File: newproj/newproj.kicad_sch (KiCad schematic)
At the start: 1 part

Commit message: Add files via upload
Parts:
- removed U?: ESP32-WROOM-32, RF_Module:ESP32-WROOM-32, symbol RF_Module:ESP32-WROOM-32
- added U?: ESP32-S3-WROOM-2, RF_Module:ESP32-S3-WROOM-2, symbol New_Library:ESP32-S3-WROOM-2
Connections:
- new net AC: U?.1 (GND), U?.26 (IO45), U?.42 (GND), U?.43 (GND)
- new net LED_CONTROL: U?.4 (IO04)
- new net TEMP SENSOR 3.3V: U?.2 (3V3)
- new net TEMP SENSOR SIGNAL: U?.34 (IO41)
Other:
- removed sheet Heater
- removed sheet Power

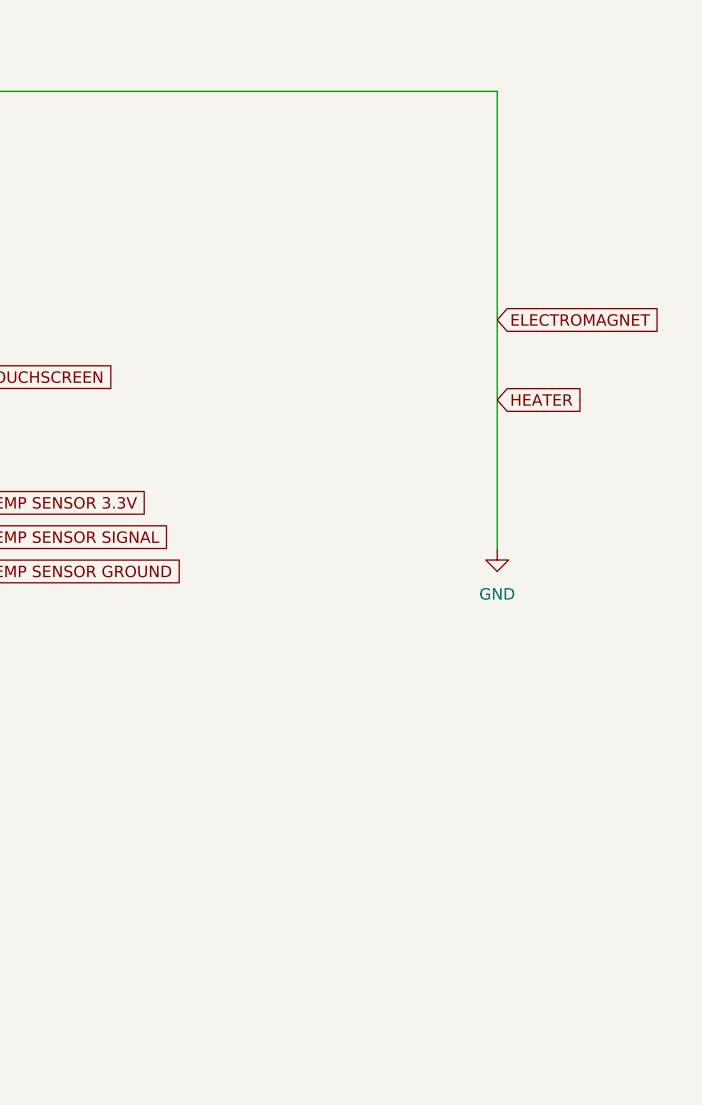
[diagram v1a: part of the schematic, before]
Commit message: Add display connector and change it in parts.txt
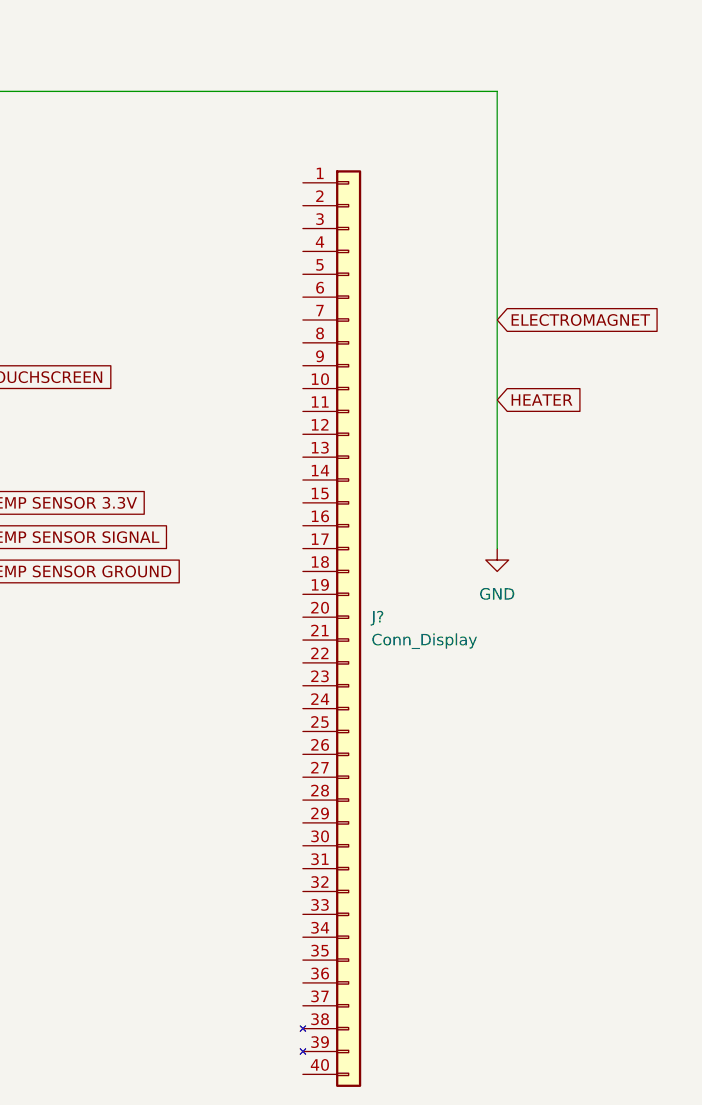
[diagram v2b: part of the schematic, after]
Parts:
- added J?: Conn_Display, symbol Conn_Display:Conn_Display
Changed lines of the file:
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@@
     )
+  )
+  (symbol (lib_id "Conn_Display:Conn_Display") (at 241.3 92.71 0) (unit 1)
+    (in_bom yes) (on_board yes) (fields_autoplaced)
+    (property "Reference" "J?" (id 0) (at 243.84 92.7099 0)
+      (effects (font (size 1.27 1.27)) (justify left))
+    )
+    (property "Value" "Conn_Display" (id 1) (at 243.84 95.2499 0)
+      (effects (font (size 1.27 1.27)) (justify left))
+    )
+    (property "Footprint" "" (id 2) (at 241.3 92.71 0)
+      (effects (font (size 1.27 1.27)) hide)
+    )
+    (property "Datasheet" "~" (id 3) (at 241.3 92.71 0)
+      (effects (font (size 1.27 1.27)) hide)
+    )
+    (pin "1")
+    (pin "10")
+    (pin "11")
+    (pin "12")
+    (pin "13")
+    (pin "14")
+    (pin "15")
+    (pin "16")
+    (pin "17")
+    (pin "18")
+    (pin "19")
+    (pin "2")
+    (pin "20")
+    (pin "21")
+    (pin "22")
+    (pin "23")
+    (pin "24")
+    (pin "25")
+    (pin "26")
+    (pin "27")
+    (pin "28")
+    (pin "29")
+    (pin "3")
+    (pin "30")
+    (pin "31")
+    (pin "32")
+    (pin "33")
+    (pin "34")
+    (pin "35")
+    (pin "36")
+    (pin "37")
+    (pin "38")
+    (pin "39")
+    (pin "4")
+    (pin "40")
+    (pin "5")
+    (pin "6")
+    (pin "7")
+    (pin "8")
+    (pin "9")
   )
   (symbol (lib_id "power:AC") (at 76.2 34.29 0) (unit 1)
@@
       (reference "#PWR?") (unit 1) (value "GND") (footprint "")
     )
+    (path "/b683e5e4-c117-4cc4-9e0d-3a6271e44c53"
+      (reference "J?") (unit 1) (value "Conn_Display") (footprint "")
+    )
     (path "/fea7b959-39c1-42ca-ad15-bc9b192cd950"

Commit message: Commit several war crimes
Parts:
- removed J?: Conn_Display, symbol Conn_Display:Conn_Display
- added C?: 22n, symbol Device:C_Small
- added C?: 2u2/6v3, symbol Device:C_Polarized_Small
- added C?: 100n, symbol Device:C_Small
- added C?: 4u7/6v3, symbol Device:C_Polarized_Small
- added J?: 40pin ZIF, symbol Connector_Generic:Conn_01x40
- added J?: AC CONN, symbol Connector:Conn_01x02_Male
- added J?: LED STRIP, symbol Connector:Conn_01x04_Female
- added J?: Thermocouple, symbol Connector:Conn_01x02_Female
- added PS?: IRM-20-12, Converter_ACDC:Converter_ACDC_MeanWell_IRM-20-xx_THT, symbol Converter_ACDC:IRM-20-12
- added PS?: IRM-10-3.3, Converter_ACDC:Converter_ACDC_MeanWell_IRM-10-xx_THT, symbol Converter_ACDC:IRM-10-3.3
- added SW?: SW_DPST, symbol Switch:SW_DPST
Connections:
- net AC: no longer names the net of U?.1 (GND), U?.26 (IO45), U?.42 (GND), U?.43 (GND)
- net LED_CONTROL: no longer names the net of U?.4 (IO04)
- net TEMP SENSOR 3.3V: no longer names the net of U?.2 (3V3)
- net TEMP SENSOR SIGNAL: no longer names the net of U?.34 (IO41)
- new net +12V: J?.1 (Pin_1), PS?.4 (+Vo)
- new net +3V3: C?.1, C?.1, C?.1, C?.1, PS?.4 (+Vo)
- new net GND: C?.2, C?.2, C?.2, C?.2, J?.4 (Pin_4), PS?.3 (-Vo), PS?.3 (-Vo)
- new net LIVE: J?.1 (Pin_1), SW?.3
- new net LIVE_SW: PS?.1 (AC/L), PS?.2 (AC/L), SW?.4
- new net NEUTRAL: J?.2 (Pin_2), SW?.1
- new net NEUTRAL_SW: PS?.1 (AC/N), PS?.2 (AC/N), SW?.2
- no-connect marks 0 -> 1
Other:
- note added: "BIGGER ONES NEAR PS MODULE SMALLER ONES NEAR ESP MODULE"
- moved on the sheet: U?

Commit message: discord is a fuck
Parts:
- added C?: 10u/16v, symbol Device:C_Polarized_Small
- added C?: 100n, symbol Device:C_Small
- added C?: 22u/16v, symbol Device:C_Polarized_Small
- added C?: 22n, symbol Device:C_Small
- added J?: UART Programming/Control, symbol Connector:Conn_01x04_Male
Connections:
- net +12V: now also C?.1, C?.1, C?.1, C?.1
- net +3V3: now also U?.2 (3V3), J?.1 (Pin_1)
- net GND: now also U?.1 (GND), U?.26 (IO45), U?.42 (GND), U?.43 (GND), C?.2, C?.2, C?.2, C?.2, J?.4 (Pin_4)
- net UART_RX: now reaches U?.36 (RXD0)
- net UART_RX: now also J?.3 (Pin_3)
- net UART_TX: now reaches U?.37 (TXD0)
- net UART_TX: now also J?.2 (Pin_2)
- no-connect marks 1 -> 4
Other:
- note added: "BIGGER ONES NEAR PS MODULE SMALLER ONES NEAR LED STRIP CONN"

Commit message: schematic + readying for pcb
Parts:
- removed J?: 40pin ZIF, symbol Connector_Generic:Conn_01x40
- removed J?: UART Programming/Control, symbol Connector:Conn_01x04_Male
- removed J?: AC CONN, symbol Connector:Conn_01x02_Male
- removed J?: LED STRIP, symbol Connector:Conn_01x04_Female
- removed J?: Thermocouple, symbol Connector:Conn_01x02_Female
- removed PS?: IRM-20-12, Converter_ACDC:Converter_ACDC_MeanWell_IRM-20-xx_THT, symbol Converter_ACDC:IRM-20-12
- removed PS?: IRM-10-3.3, Converter_ACDC:Converter_ACDC_MeanWell_IRM-10-xx_THT, symbol Converter_ACDC:IRM-10-3.3
- removed U?: ESP32-S3-WROOM-2, RF_Module:ESP32-S3-WROOM-2, symbol New_Library:ESP32-S3-WROOM-2
- added C1, C13, C2, C3: 2u2/6v3, Capacitor_SMD:CP_Elec_4x3, symbol Device:C_Polarized_Small
- added C12, C18, C4, C5, C6: 100n, Capacitor_SMD:C_0603_1608Metric, symbol Device:C_Small
- added C7: 10u/16v, Capacitor_SMD:CP_Elec_6.3x3.9, symbol Device:C_Polarized_Small
- added D1: 1N4002, Diode_SMD:D_SMA, symbol Device:D
- added F1, F2: 10A, Fuse:Fuseholder_Clip-5x20mm_Littelfuse_520_Inline_P20.50x5.80mm_D1.30mm_Horizontal, symbol Device:Fuse
- added J1: SWD, Connector_PinHeader_2.54mm:PinHeader_1x04_P2.54mm_Vertical, symbol Connector_Generic:Conn_01x04
- added J2: AC CONN, TerminalBlock:TerminalBlock_bornier-2_P5.08mm, symbol Connector:Screw_Terminal_01x02
- added J3: TOUCH DISPLAY, Connector_PinHeader_2.54mm:PinHeader_1x14_P2.54mm_Vertical, symbol Connector_Generic:Conn_01x14
- added J5: Thermocouple, TerminalBlock:TerminalBlock_bornier-2_P5.08mm, symbol Connector:Screw_Terminal_01x02
- added J6: Higher Heater, TerminalBlock:TerminalBlock_bornier-2_P5.08mm, symbol Connector:Screw_Terminal_01x02
- added J7: Lower Heater, TerminalBlock:TerminalBlock_bornier-2_P5.08mm, symbol Connector:Screw_Terminal_01x02
- added J8: Electromagnet, TerminalBlock:TerminalBlock_bornier-2_P5.08mm, symbol Connector:Screw_Terminal_01x02
- added J9: LED STRIP, Connector_PinHeader_2.54mm:PinHeader_1x03_P2.54mm_Vertical, symbol Connector_Generic:Conn_01x03
- added PS1: IRM-10-3.3, Converter_ACDC:Converter_ACDC_MeanWell_IRM-10-xx_THT, symbol Converter_ACDC:IRM-10-3.3
- added PS2: IRM-02-12, Converter_ACDC:Converter_ACDC_MeanWell_IRM-02-xx_THT, symbol Converter_ACDC:IRM-02-12
- added PS3: IRM-20-5, Converter_ACDC:Converter_ACDC_MeanWell_IRM-20-xx_THT, symbol Converter_ACDC:IRM-20-5
- added Q1, Q2: BT139-600, Package_TO_SOT_THT:TO-220-3_Vertical, symbol Triac_Thyristor:BT139-600
- added Q3: BS107, Package_TO_SOT_THT:TO-92_Inline, symbol Transistor_FET:BS107
- added R1, R2, R3, R4, R5, R6: 220R, Resistor_SMD:R_0603_1608Metric, symbol Device:R
- added R7, R8: 10k, Resistor_SMD:R_0603_1608Metric, symbol Device:R
- added SW2: PROJECT ~{RESET}, Button_Switch_SMD:SW_SPST_PTS645, symbol Switch:SW_Push
- added U1: HC-05, HC-05:XCVR_HC-05, symbol HC-05:HC-05
- added U2, U3: MOC3041M, Package_DIP:DIP-6_W7.62mm, symbol Relay_SolidState:MOC3041M
- added U4: ATSAML21G16B-AUT, Package_QFP:TQFP-48_7x7mm_P0.5mm, symbol MCU_Microchip_SAML:ATSAML21G16B-AUT
- C10, C16: renamed from C?; footprint (none) -> Capacitor_SMD:C_0603_1608Metric
- C11, C17: renamed from C?; value 22n -> 100n; footprint (none) -> Capacitor_SMD:C_0603_1608Metric
- C14: renamed from C?; footprint (none) -> Capacitor_SMD:CP_Elec_4x3
- C15: renamed from C?; value 4u7/6v3 -> 2u2/6v3; footprint (none) -> Capacitor_SMD:CP_Elec_4x3
- C8: renamed from C?; value 22u/16v -> 10u/16v; footprint (none) -> Capacitor_SMD:CP_Elec_6.3x3.9
- C9: renamed from C?; footprint (none) -> Capacitor_SMD:CP_Elec_6.3x3.9
- SW1: renamed from SW?; value SW_DPST -> PWR SWITCH; footprint (none) -> Connector_PinHeader_2.54mm:PinHeader_1x04_P2.54mm_Vertical
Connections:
- net +12V: now also D1.1 (K), J8.1 (Pin_1), PS2.4 (+Vo), Q3.1 (D); no longer C10.1, C11.1, C8.1, C9.1
- net +3V3: now also C1.1, C13.1, C2.1, C3.1, C4.1, C5.1, J1.1 (Pin_1), J3.8 (Pin_8), PS1.4 (+Vo), R7.1, U1.12 (3.3_VCC), U4.17 (VDDIO), U4.36 (VDDIO), U4.44 (VDDIN), U4.6 (VDDANA)
- net GND: now also C1.2, C12.2, C13.2, C18.2, C2.2, C3.2, C4.2, C5.2, C6.2, C7.2, J1.4 (Pin_4), J3.2 (Pin_2), J9.3 (Pin_3), PS1.3 (-Vo), PS2.3 (-Vo), PS3.3 (-Vo), Q3.3 (S), R3.1, R6.1, R8.2, SW2.1, U1.13 (GND), U1.21 (GND), U1.22 (GND), U4.18 (GND), U4.35 (GND), U4.42 (GND), U4.5 (GNDANA)
- net LIVE: now also J2.1 (Pin_1)
- net LIVE_SW: now also J6.1 (Pin_1), J7.1 (Pin_1), PS1.2 (AC/L), PS2.2 (AC/L), PS3.1 (AC/L), Q1.2 (A2), Q2.2 (A2), R1.2, R4.2
- net NEUTRAL: now also J2.2 (Pin_2)
- net NEUTRAL_SW: now also F1.1, F2.1, PS1.1 (AC/N), PS2.1 (AC/N), PS3.2 (AC/N), Q1.1 (A1), Q2.1 (A1)
- new net: C18.1, U4.41 (VDDCORE)
- new net: R1.1, U2.6
- new net: F1.2, J6.2 (Pin_2)
- new net: Q2.3 (G), R5.2
- new net: R6.2, U3.2
- new net: R5.1, U3.4
- new net: R4.1, U3.6
- new net: D1.2 (A), J8.2 (Pin_2)
- new net: R2.1, U2.4
- new net: Q1.3 (G), R2.2
- new net: R3.2, U2.2
- new net: F2.2, J7.2 (Pin_2)
- new net +5V: C10.1, C11.1, C12.1, C6.1, C7.1, C8.1, C9.1, J3.1 (Pin_1), J9.1 (Pin_1), PS3.4 (+Vo)
- new net CLK: J3.10 (Pin_10), U4.26 (PA17)
- new net DC/RS: J3.5 (Pin_5), U4.27 (PA18)
- new net EM_SW: Q3.2 (G), R8.1, U4.13 (PA08)
- new net HH_PWM: U2.1, U4.15 (PA10)
- new net LED_DIN: J9.2 (Pin_2), U4.14 (PA09)
- new net LH_PWM: U3.1, U4.16 (PA11)
- new net MISO: J3.13 (Pin_13), J3.9 (Pin_9), U4.25 (PA16)
- new net MOSI: J3.12 (Pin_12), J3.6 (Pin_6), U4.24 (PA15)
- new net RX_BT: U1.2 (UART-RX), U4.22 (PA13)
- new net SCK: J3.7 (Pin_7), U4.12 (PA07)
- new net SWCLK: J1.3 (Pin_3), U4.45 (PA30)
- new net SWDIO: J1.2 (Pin_2), U4.46 (PA31)
- new net TH+: J5.1 (Pin_1), U4.11 (PA06)
- new net TH-: J5.2 (Pin_2), U4.3 (PA02)
- new net TX_BT: U1.1 (UART-TX), U4.21 (PA12)
- new net T_DETECT: J3.14 (Pin_14), U4.31 (PA22)
- new net ~{CS}_DISP: J3.3 (Pin_3), U4.28 (PA19)
- new net ~{CS}_T: J3.11 (Pin_11), U4.29 (PA20)
- new net ~{RST}: R7.2, SW2.2, U4.40 (~{RESET})
- new net ~{RST}_BT: U1.11 (~{RESETB}), U4.23 (PA14)
- new net ~{RST}_LCD: J3.4 (Pin_4), U4.30 (PA21)
- no-connect marks 4 -> 44
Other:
- note added: "BIGGER ONES NEAR PS MODULE SMALLER ONES NEAR 3V3 BT POWER PIN"
- note added: "BIGGER ONES NEAR PS MODULE SMALLER ONES NEAR VDDIO, VDDANA AND VDDCORE"
- note added: "E TYPE (68 µV/°C) BECAUSE OF MAGNETIC FIELD NEAR TOASTER"
- note added: "TH- and TH+ are inputs to built-in Op-Amp in MCU. This OA is software-controllable. IMPORTANT: KEEP TH+/- LINES AWAY FROM DIGITAL LINES AS MUCH AS POSSIBLE"
- note removed: "BIGGER ONES NEAR PS MODULE SMALLER ONES NEAR ESP MODULE"
- moved on the sheet: C10, C11, C14, C15, C16, C17, C8, C9, SW1

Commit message: pcb layout draft
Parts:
- removed U1: HC-05, HC-05:XCVR_HC-05, symbol HC-05:HC-05
- added J5: HC MODULE, Connector_PinHeader_2.54mm:PinHeader_1x04_P2.54mm_Vertical, symbol Connector_Generic:Conn_01x04
- J2: renamed from J9; footprint Connector_PinHeader_2.54mm:PinHeader_1x03_P2.54mm_Vertical -> Connector_Molex:Molex_Micro-Fit_3.0_43650-0315_1x03_P3.00mm_Vertical
- renumbered C7 to C1, C16 to C10, C17 to C11, C18 to C12, C1 to C13, C2 to C14, C3 to C15, C4 to C16, C5 to C17, C6 to C18, C8 to C2, C9 to C3, C10 to C4, C11 to C5, C12 to C6, C13 to C7, C14 to C8, C15 to C9, J2 to J1, J1 to J3, J5 to J4, J3 to J8, J8 to J9, U2 to U1, U3 to U2, U4 to U3
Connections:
- net +12V: no longer Q3.1 (D)
- net +3V3: now also J5.1 (Pin_1)
- net GND: now also J5.4 (Pin_4)
- net RX_BT: now also J5.2 (Pin_2)
- net TX_BT: now also J5.3 (Pin_3)
- net at D1.2 (A), J9.2 (Pin_2): now also Q3.1 (D)
- net ~{RST}_BT: no longer names the net of U3.23 (PA14)
- no-connect marks 44 -> 19
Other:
- moved on the sheet: D1, J9
